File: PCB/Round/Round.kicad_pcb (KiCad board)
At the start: 2 copper layers, 46 x 46 mm, 50 parts, among them J3 Conn, SW1 ESE13V01D, U1 PN532, U2 QR, Y1 27.12MHz

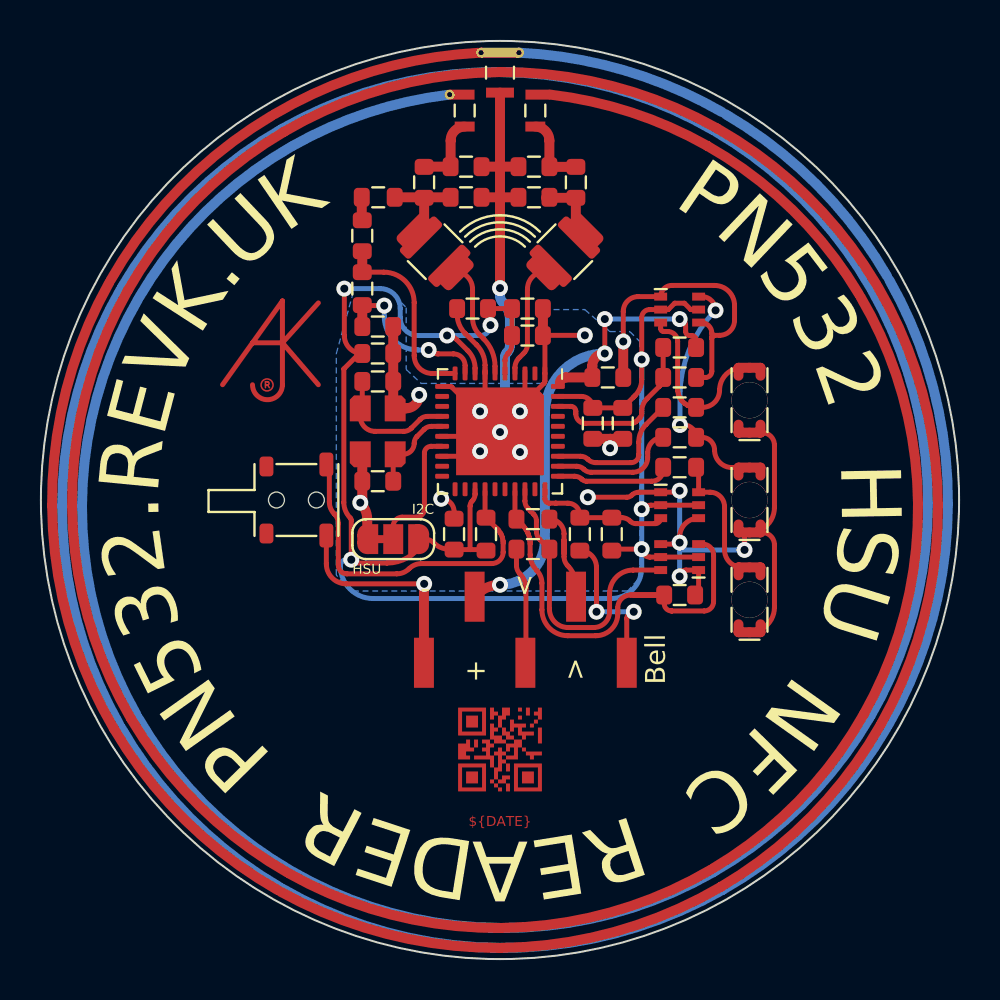
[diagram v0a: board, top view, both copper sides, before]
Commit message: Production nearly ready - may have to change to square LEDs.
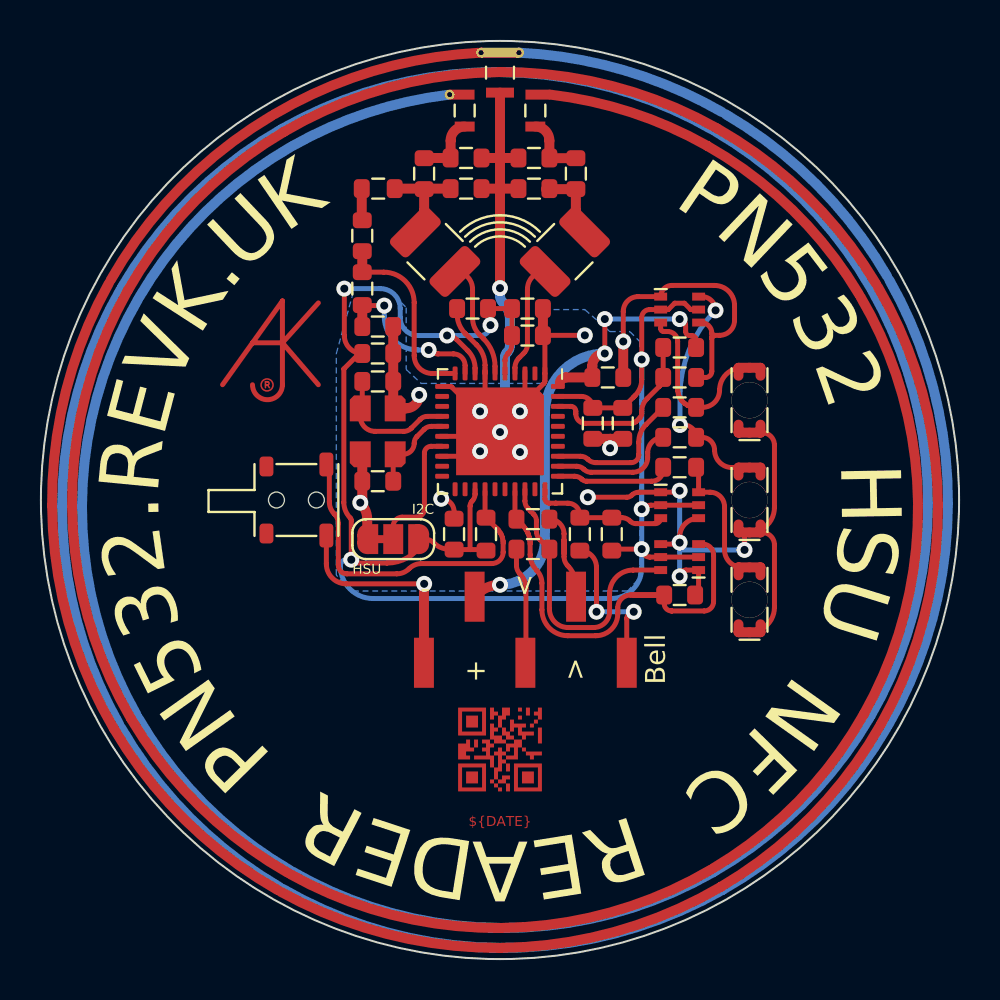
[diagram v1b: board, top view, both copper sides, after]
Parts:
- L1, L2: footprint RevK:L_1206_1008 -> Inductor_SMD:L_1210_3225Metric
- R4: value 2K7 1% -> 2k7 1%
- R5: value 1K 1% -> 1k 1%
- moved C1 0.44 mm to (101.7, 82.9)
- moved C2 0.44 mm to (98.3, 82.9)
- moved C3 0.43 mm to (103.8, 83.7)
- moved C4 0.43 mm to (96.2, 83.7)
- moved C5 0.43 mm to (101.7, 84.4)
- moved C6 0.43 mm to (98.3, 84.4)
- moved R4 0.43 mm to (93.9, 84.4)

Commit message: production for LEDs as well
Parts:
- D1, D2, D3: footprint RevK:STP_156120xx7530 -> RevK:LED_1206_Rev_Square
- L1, L2: footprint Inductor_SMD:L_1210_3225Metric -> Inductor_SMD:L_1008_2520Metric
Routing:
- net GND: track 115.1 -> 115.6 mm, vias 18 -> 20
